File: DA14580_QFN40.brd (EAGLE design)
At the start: 92 x 73 mm, 31 parts, among them CON1 CON_TC2030-CTL-NL, IC1 IC_MEMORY_8P_AT25XE011_SOP, IC2 NC7SZ00M5XCT-ND, IC3 LDO5_3.3_SOT23, Q1 32.768k, Q2 16M/2520, U1 DA14583AT2, X1 SSW-114-02-S-S, X2 SSW-114-02-S-S

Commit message: [ 58x ] font alignment
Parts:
- GIT1: value (none) -> b61e68f
- ICON1: device mylib:ICON_REVISION -> mylib:ICON_REVISION1.2
- TP3: value TPPAD1-13 -> (none); device testpad_local:P1-13 -> mylib:TP_4020
- moved ICON1 44.8 mm to (31.9, 14.0)
- moved GIT1 14.9 mm to (0.00, 0.00)
- moved TP3 1.88 mm to (31.8, 11.8)
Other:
- board text removed: "v0.5"

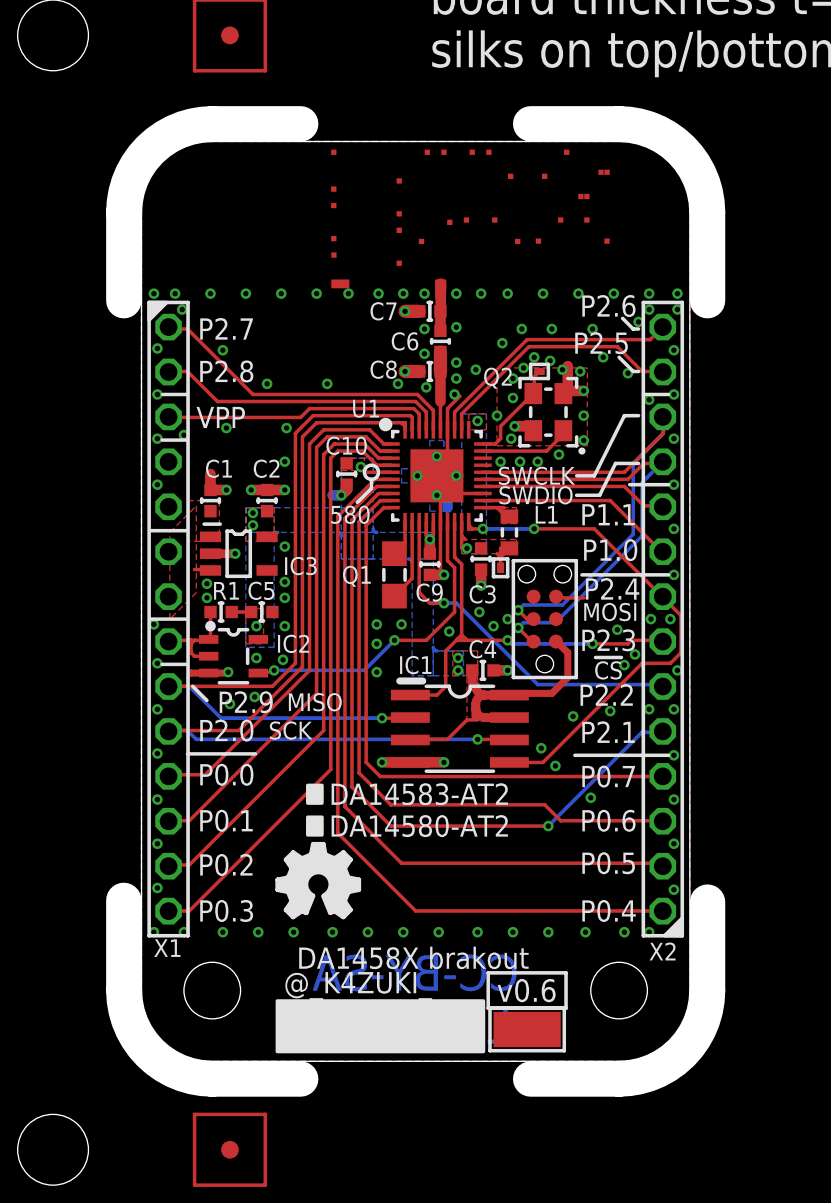
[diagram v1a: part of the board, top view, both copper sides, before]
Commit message: replace IC2/3 to smaller outlined devices
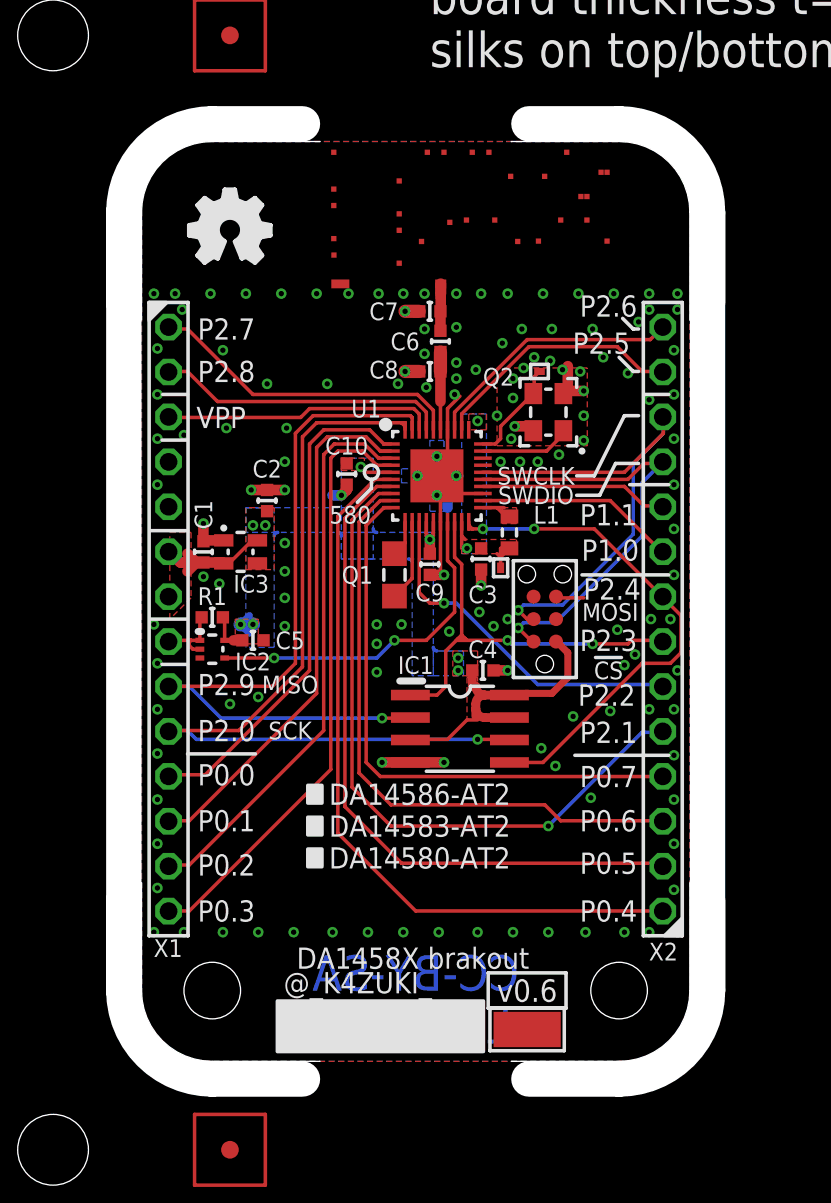
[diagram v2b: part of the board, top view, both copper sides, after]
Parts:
- added P1, P2: (no value), mylib:PCB_CORNER_NH
- added P3, P4: (no value), mylib:PCB_CORNER
- IC2: value NC7SZ00M5XCT-ND -> (none); device 74xx-little-us_local:SOT23-5 -> mylib:SOT50P160X120-5N
- IC3: value LDO5_3.3_SOT23 -> (none); device mylib:IC_05_0.95_50MIL -> mylib:SOT130P220X135-4N
- moved U$2 37.3 mm to (15.0, 57.0)
- moved C1 2.93 mm to (13.5, 38.8)
- moved C5 1.68 mm to (16.3, 33.8)
- moved IC2 1.26 mm to (14.0, 33.3)
- moved R1 0.58 mm to (14.0, 35.1)
- moved IC3 0.14 mm to (15.6, 38.8)
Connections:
- net GND: now also IC3.1; no longer IC3.2
- net VCC: now also IC3.3; no longer IC3.5
- net VDD: now also IC3.2, IC3.4; no longer IC3.1, IC3.3
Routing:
- net VDD: track 0.92 -> 7.28 mm
- net GND: track 41.3 -> 36.0 mm, vias 148 -> 144
- net VCC: track 24.7 -> 28.1 mm, vias 7 -> 8
- net !RESET!: track 6.26 -> 4.41 mm
- net RESET: track 17.8 -> 19.3 mm
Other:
- outline, holes or cut-outs redrawn
- board text added: "DA14586-AT2 DA14583-AT2 DA14580-AT2"
- board text removed: "DA14583-AT2 DA14580-AT2"
